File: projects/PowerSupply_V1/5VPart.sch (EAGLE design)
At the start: 15 parts, among them IC1 LM2596T, IC2 LM2991, X1 IN

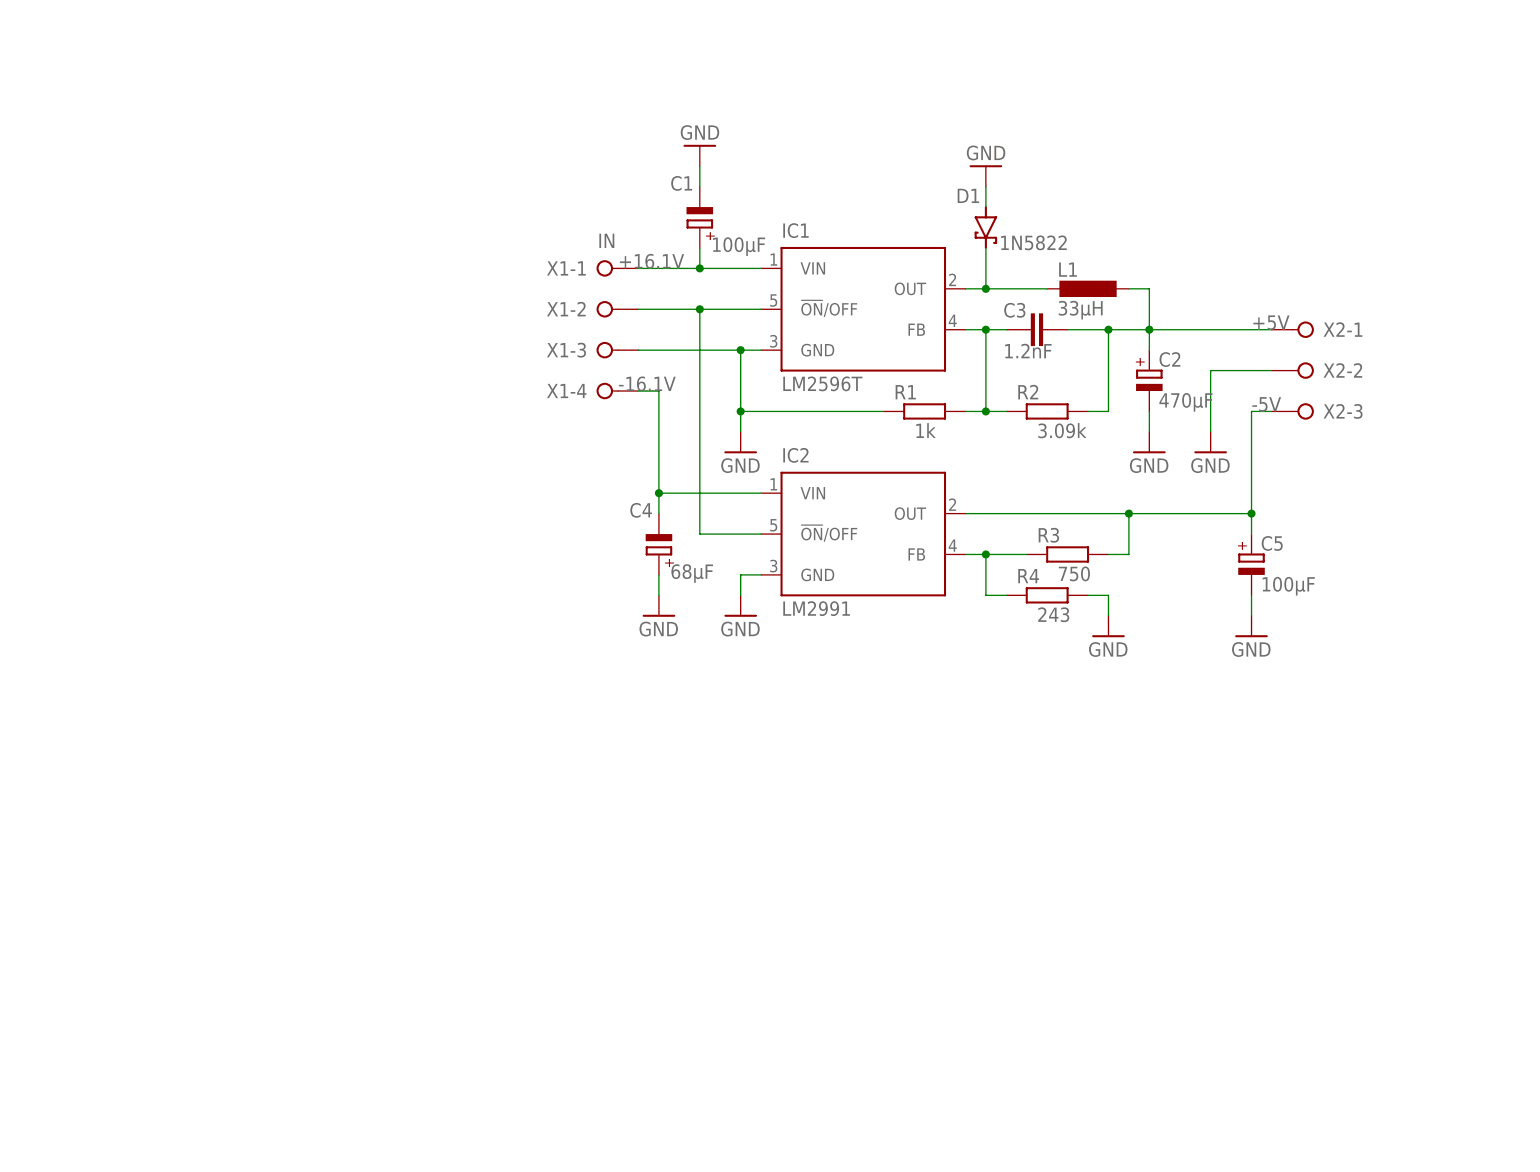
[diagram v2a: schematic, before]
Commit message: feat: 5V part refactored
changes:
- schematic changed
- layout changed
- gerber files added
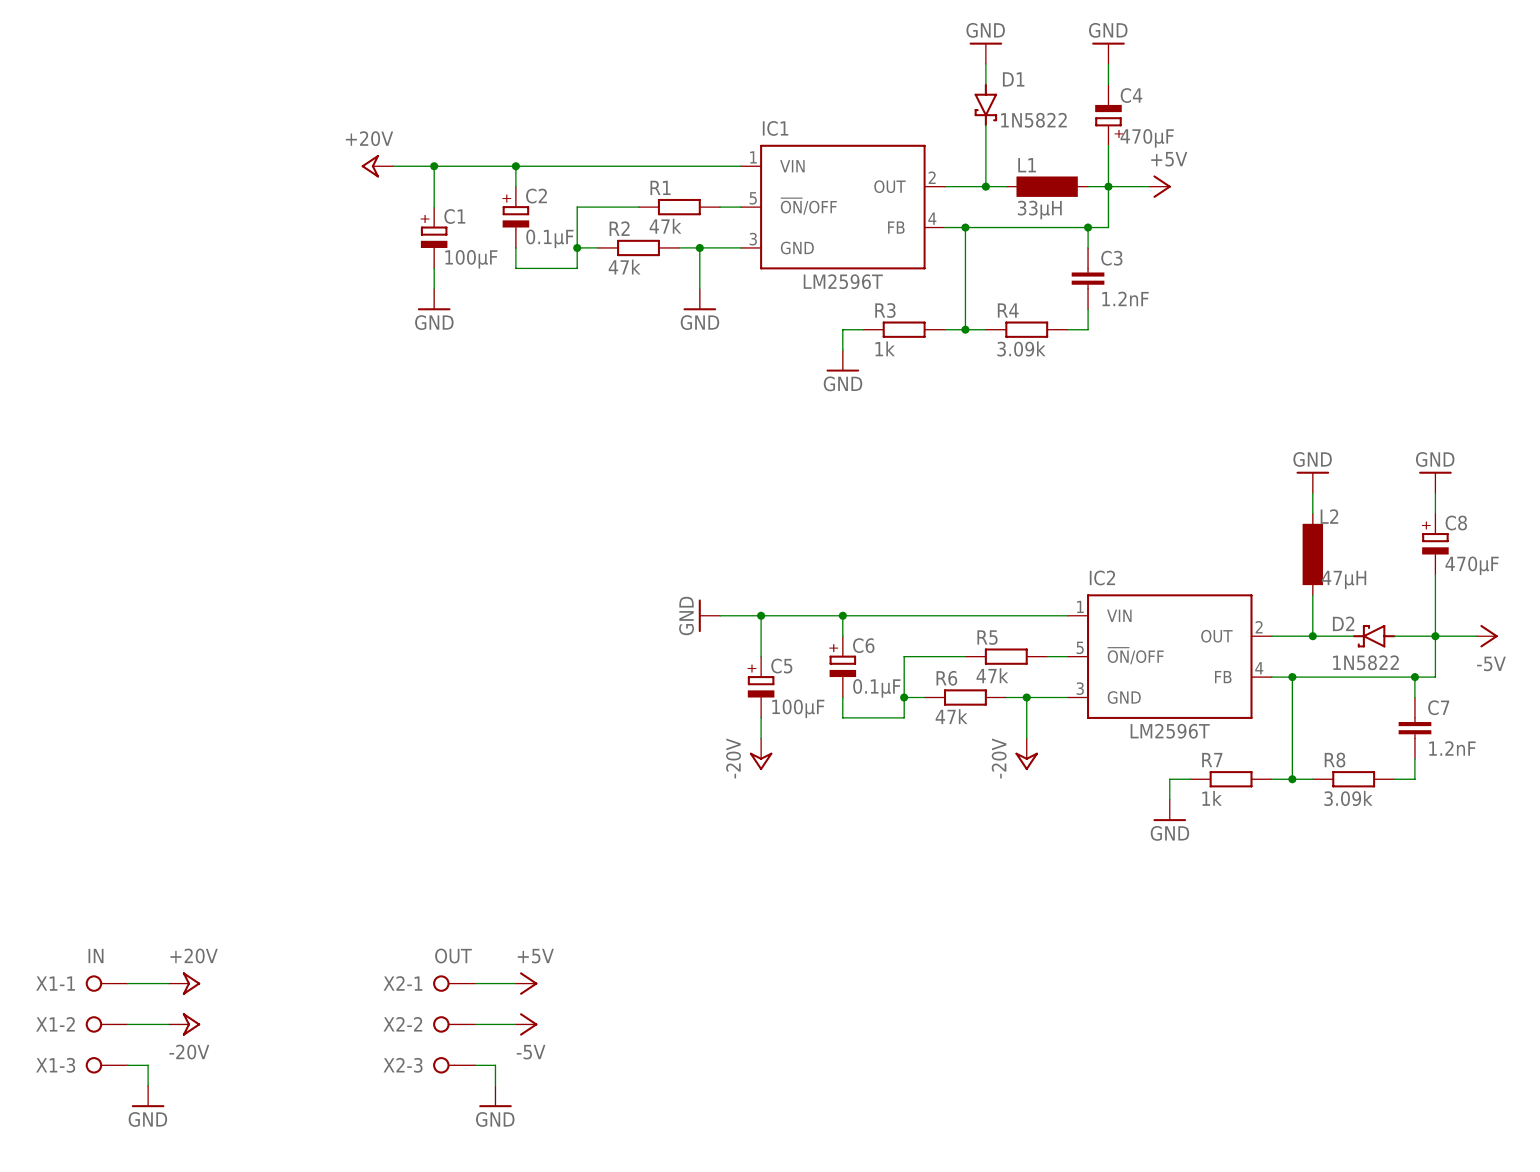
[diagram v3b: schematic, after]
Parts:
- added C6: 0.1µF, rcl:CPOL-EUE1.8-4
- added C7: 1.2nF, rcl:C-EU050-024X044
- added C8: 470µF, rcl:CPOL-EUE3.5-8
- added D2: 1N5822, diode:SCHOTTKY-DIODEC4111-15
- added L2: 47µH, inductor-neosid:SD12-680
- added R5, R6: 47k, rcl:R-EU_0207/10
- added R7: 1k, rcl:R-EU_0207/10
- added R8: 3.09k, rcl:R-EU_0207/10
- C2: value 470µF -> 0.1µF; device rcl:CPOL-EUE2.5-6 -> rcl:CPOL-EUE1.8-4
- C4: value 68µF -> 470µF; device rcl:CPOL-EUE2-5 -> rcl:CPOL-EUE3.5-8
- C5: device rcl:CPOL-EUE2-5 -> rcl:CPOL-EUE2.5-6
- IC2: value LM2991 -> LM2596T
- L1: device rcl:L-EUTJ3-U2 -> inductor-neosid:SD12-680
- R1: value 1k -> 47k
- R2: value 3.09k -> 47k
- R3: value 750 -> 1k
- R4: value 243 -> 3.09k
- X1: device con-wago-508:W237-04P -> con-wago-508:W237-03P
- X2: value (none) -> OUT
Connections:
- removed net +16.1V: C1.+, IC1.VIN, X1-1.KL
- removed net -16.1V: C4.-, IC2.VIN, X1-4.KL
- new net +24V: C1.+, C2.+, IC1.VIN, X1-1.KL
- new net -24V: C5.-, IC2.GND, R6.2, X1-2.KL
- new net N$5: C7.2, R8.2
- new net N$6: C2.-, R1.1, R2.1
- new net N$7: IC2.!ON!/OFF, R5.2
- new net N$8: C6.-, R5.1, R6.1
- net +5V: now also C3.1, C4.+, IC1.FB, L1.2, R3.2, R4.1; no longer C2.+, C3.2, L1.1, R2.2
- net -5V: now also C7.1, C8.-, D2.A, IC2.FB, R7.2, R8.1, X2-2.KL; no longer C5.+, IC2.OUT, R3.2, X2-3.KL
- net GND: now also C4.-, C5.+, C6.+, C8.+, IC2.VIN, L2.2, R2.2, R3.1, R7.1, X2-3.KL; no longer C2.-, C4.+, C5.-, IC2.GND, R1.1, R4.2, X2-2.KL
- net N$1: now also C3.2, R4.2; no longer C3.1, IC1.FB, R1.2, R2.1
- net N$2: now also D2.C, IC2.OUT, L2.1; no longer IC1.!ON!/OFF, IC2.!ON!/OFF, X1-2.KL
- net N$3: now also D1.C, IC1.OUT, L1.1; no longer IC2.FB, R3.1, R4.1
- net N$4: now also IC1.!ON!/OFF, R1.2; no longer D1.C, IC1.OUT, L1.2
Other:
- moved on the sheet: C1, C2, C3, C4, C5, D1, IC1, IC2, L1, R1, R2, R3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

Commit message: refactor(5v): schematics changed
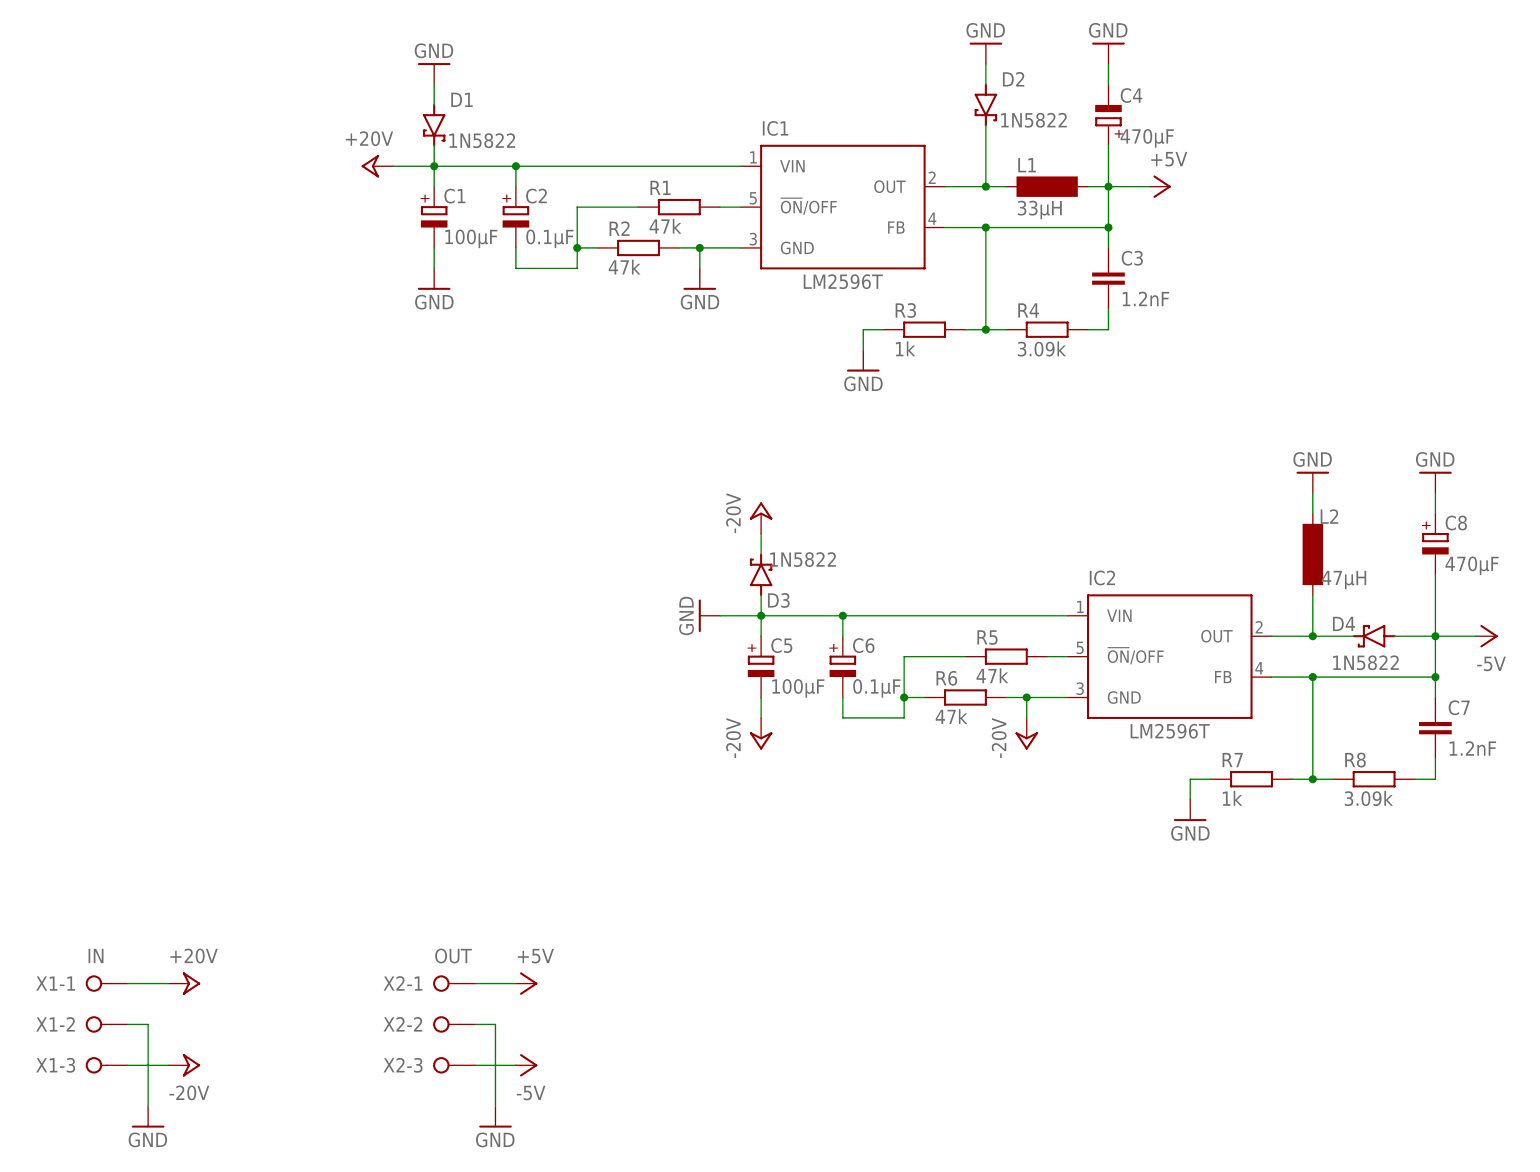
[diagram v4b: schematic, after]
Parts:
- added D3, D4: 1N5822, diode:SCHOTTKY-DIODEC4111-15
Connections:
- net +24V: now also D1.C
- net -24V: now also D3.C, X1-3.KL; no longer X1-2.KL
- net -5V: now also D4.A, X2-3.KL; no longer D2.A, X2-2.KL
- net GND: now also D2.A, D3.A, X1-2.KL, X2-2.KL; no longer X1-3.KL, X2-3.KL
- net N$2: now also D4.C; no longer D2.C
- net N$3: now also D2.C; no longer D1.C
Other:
- moved on the sheet: C1, C3, C5, C7, D1, D2, R3, R4, R7, R8
